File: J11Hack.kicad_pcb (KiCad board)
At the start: 2 copper layers, 200 x 100 mm, 86 parts, among them J1 SLU0, J2 SLU1, J3 5V, Q1 AO3401A, SW1 HMOD/BSEL, SW2 Init, SW3 Halt, SW4 Rate, SW5 Boot Sel, SW6 Power, U1 DCJ11-AE, U10 HD-6402_{B}, U11 AY-5-8116, U12 AS6C4008, U13 AS6C4008, U14 AS6C4008, U15 AS6C4008, U16 ROM_{L}, U18 ROM_{H}, U2 74HCT573, U21 BOOT_{L}, U22 BOOT_{H}, U3 74HCT573, U4 74HCT573, U5 22V10_{MEM}, U6 22V10_{IO}, U7 74HCT573, U8 22V10_{PWR}, U9 HD-6402_{A}, Y2 ~10MHz, Y3 5.0688MHz

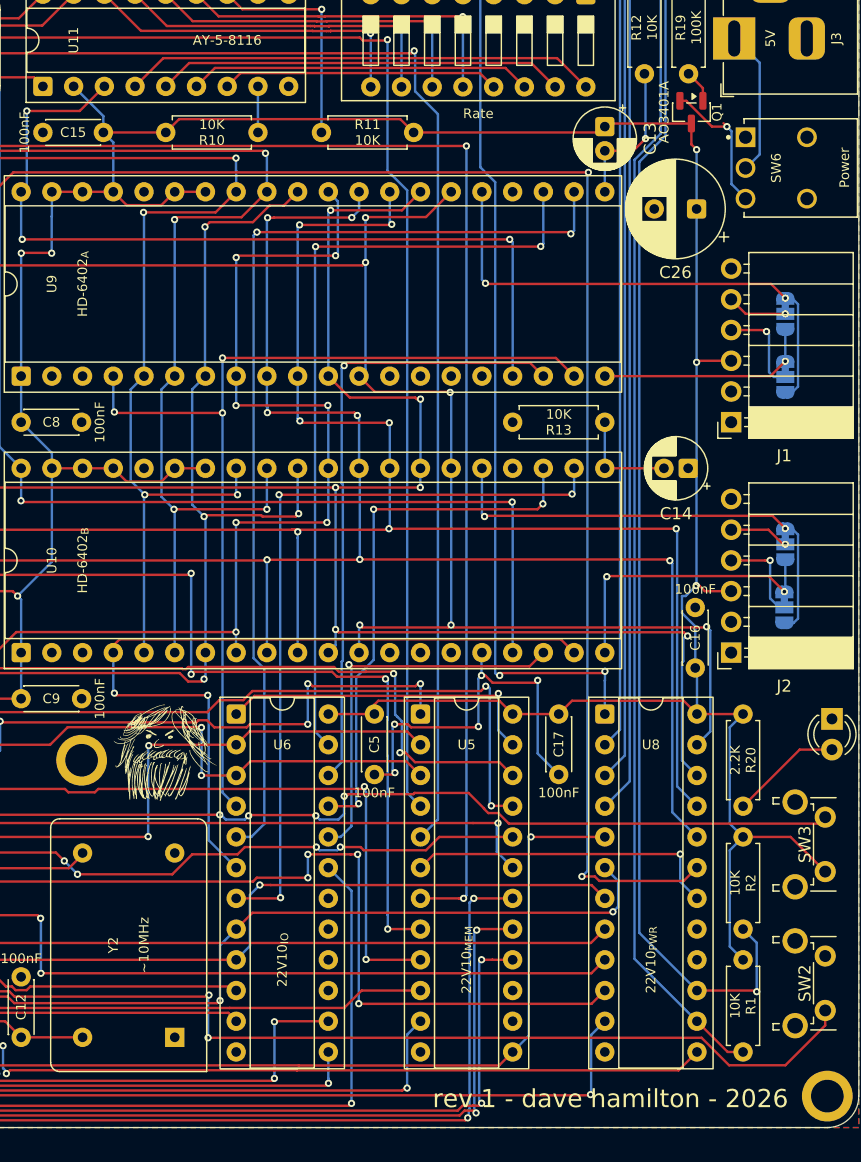
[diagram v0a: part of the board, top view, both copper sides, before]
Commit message: get the GALs working with GALasm
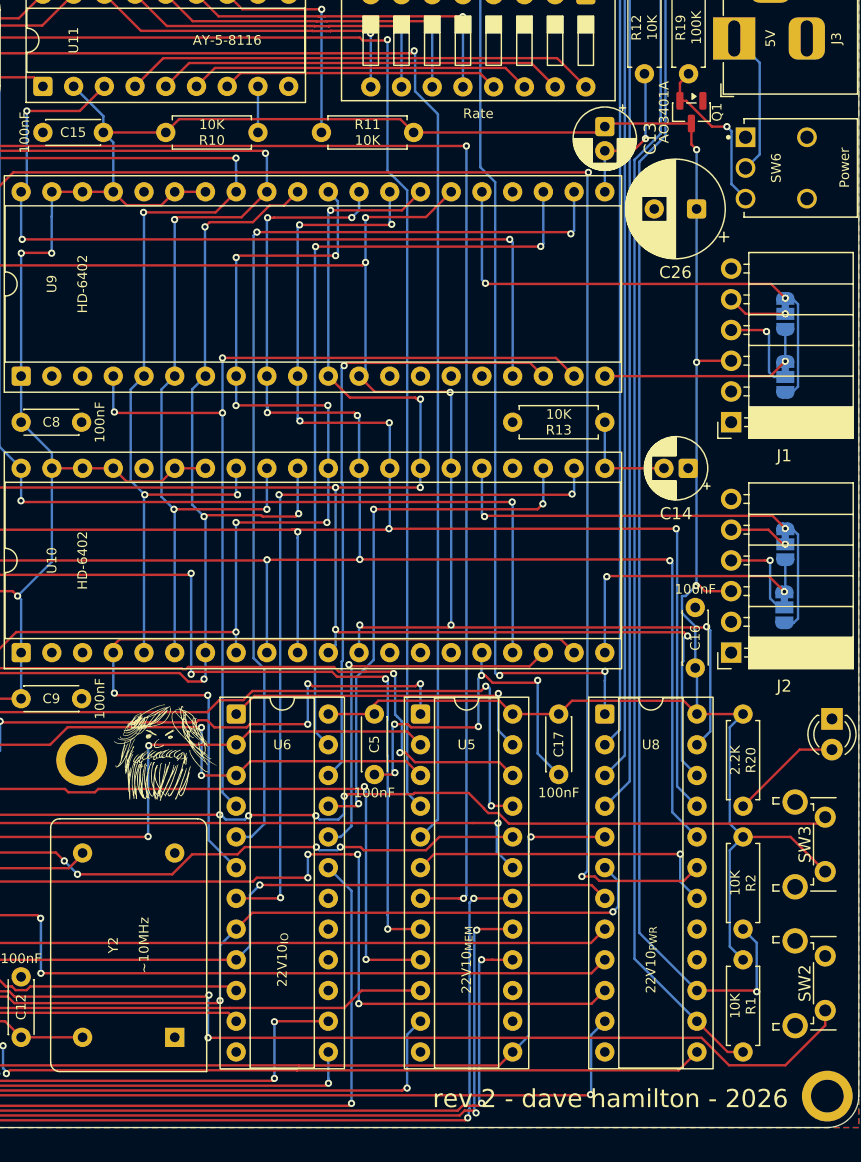
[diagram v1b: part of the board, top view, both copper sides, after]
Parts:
- U10: value HD-6402_{B} -> HD-6402
- U9: value HD-6402_{A} -> HD-6402
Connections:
- Q1 pad 1: Net-(Q1-G) -> GND
- R19 pad 1: Net-(Q1-G) -> Net-(Q1-S)
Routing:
- net Net-(Q1-G): track 2.73 -> 0.00 mm
- net Net-(Q1-S): track 11.8 -> 13.9 mm
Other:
- board text added: "rev 2 - dave hamilton - 2026"
- board text removed: "rev 1 - dave hamilton - 2026"
